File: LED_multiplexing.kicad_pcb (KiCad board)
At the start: 2 copper layers, 39.4 x 41.9 mm, 15 parts, among them J1 CONN_01X05, Q1 3906, Q2 3906, Q3 3906, U1 74HC595

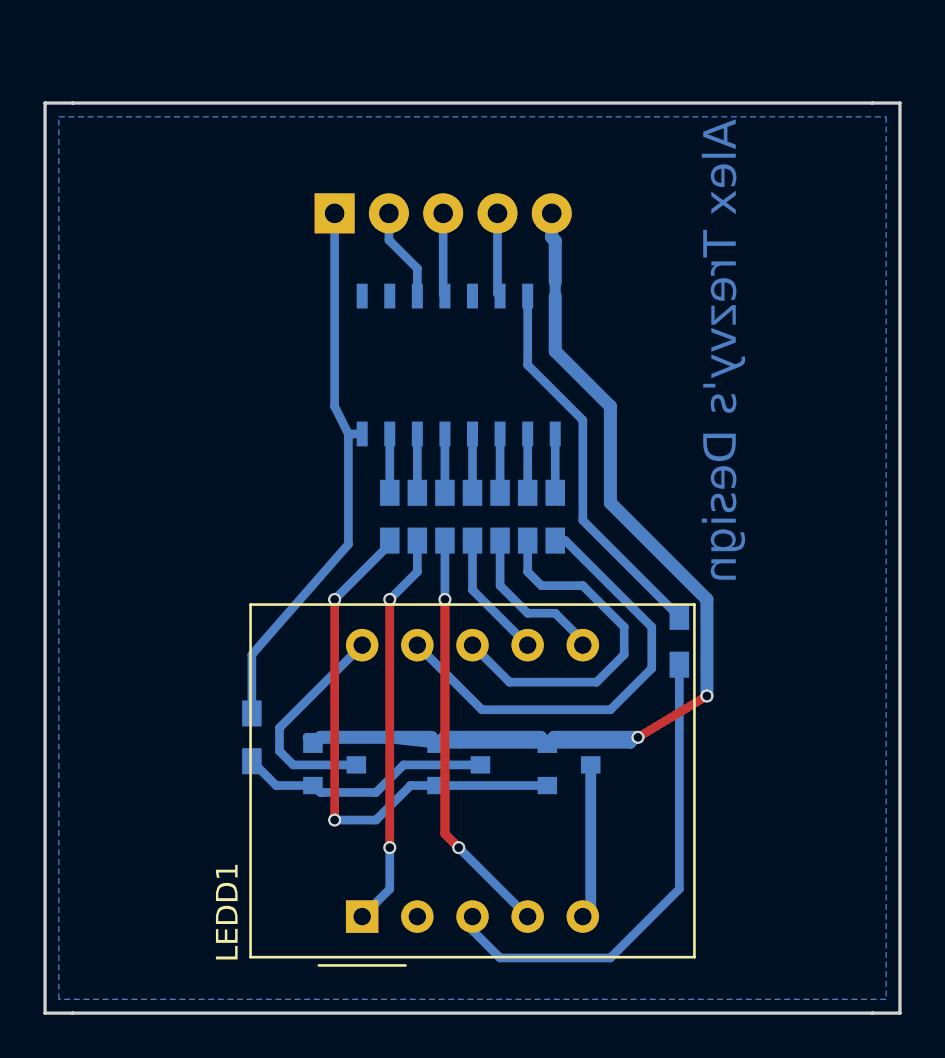
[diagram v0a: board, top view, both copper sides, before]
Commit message: made capacitors larger
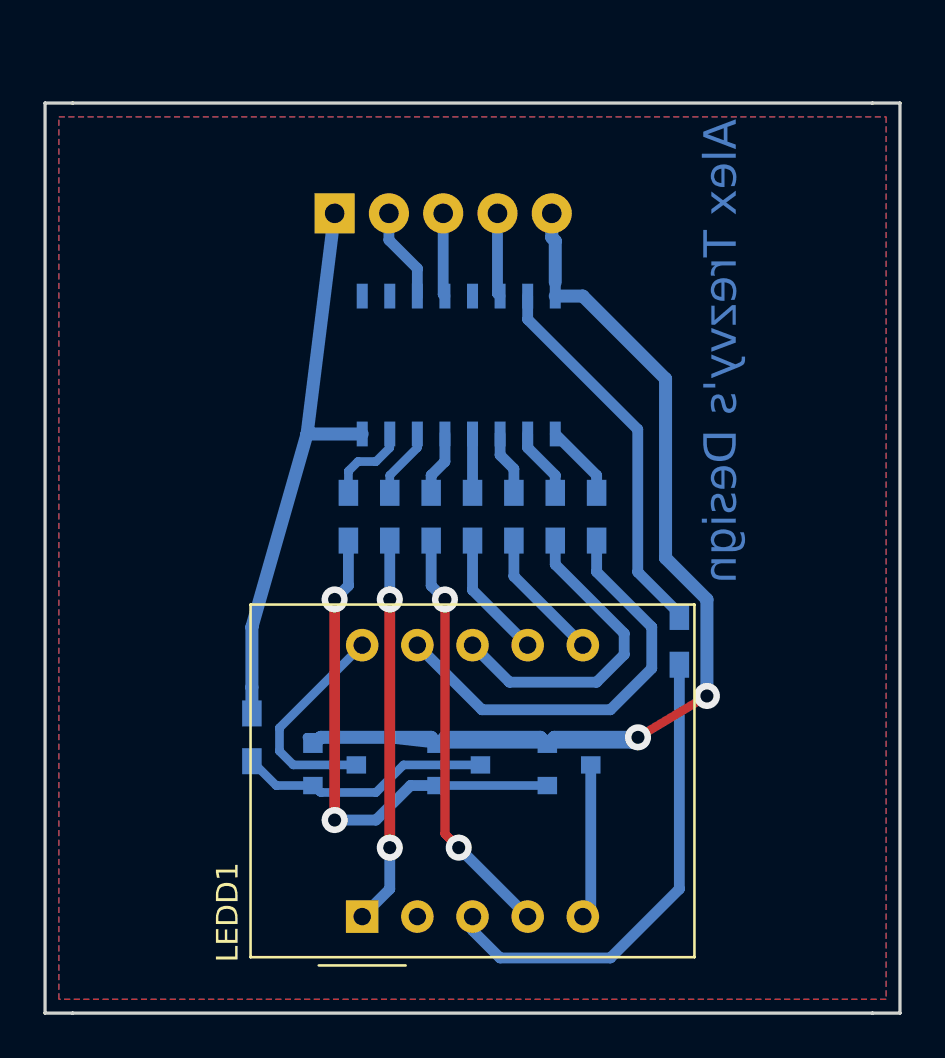
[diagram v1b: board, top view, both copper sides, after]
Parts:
- moved R1 1.91 mm to (202.6, 135.3)
- moved R7 1.91 mm to (214.0, 135.3)
- moved R10 1.27 mm to (204.5, 135.3)
- moved R6 1.27 mm to (212.1, 135.3)
- moved R4 0.63 mm to (206.4, 135.3)
- moved R9 0.63 mm to (210.2, 135.3)
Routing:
- net VCC: track 81.3 -> 67.7 mm
- net Net-(LEDD1-Pad8): track 16.4 -> 14.8 mm
- net Net-(R1-Pad1): track 2.71 -> 3.99 mm
- net Net-(LEDD1-Pad9): track 20.8 -> 19.8 mm
- net Net-(LEDD1-Pad6): track 7.34 -> 6.33 mm
- net Net-(R7-Pad2): track 2.71 -> 3.50 mm
- net Net-(Q1-Pad1): track 24.4 -> 23.6 mm
- net Net-(R6-Pad2): track 2.71 -> 3.24 mm
- net Net-(R10-Pad2): track 2.71 -> 3.24 mm
- net Net-(LEDD1-Pad1): track 18.4 -> 17.8 mm
- net GND: track 25.5 -> 26.0 mm
- added copper zone on F.Cu, net (none)
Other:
- net class Default: clearance 0.25 -> 0.2
- net class power: clearance 0.25 -> 0.2
- rule trace_clearance: 0.25 -> 0.2
- rule via_min_size: 0.4 -> 0.6
